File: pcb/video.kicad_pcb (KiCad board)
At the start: 4 copper layers, 159.9 x 99.9 mm, 174 parts, among them J1 09031966921, J3 Conn_01x06, J4 Conn_01x06, J5 Conn_01x06, J6 Conn_01x06, J7 DB15_Female_HighDensity, J8 HDMI_A, U1 NCP115, U10 NCA9306DPH, U2 LP3853ESX-3.3/NOPB, U3 LCMXO2-1200HC-4TG100I, U4 LCMXO2-7000HC-4TG144C, U5 THS8136, U6 TFP410PAP, U7 ESD224DQA, U8 ESD224DQA, U9 PCA9540BDP, X1 ASV-xxxMHz

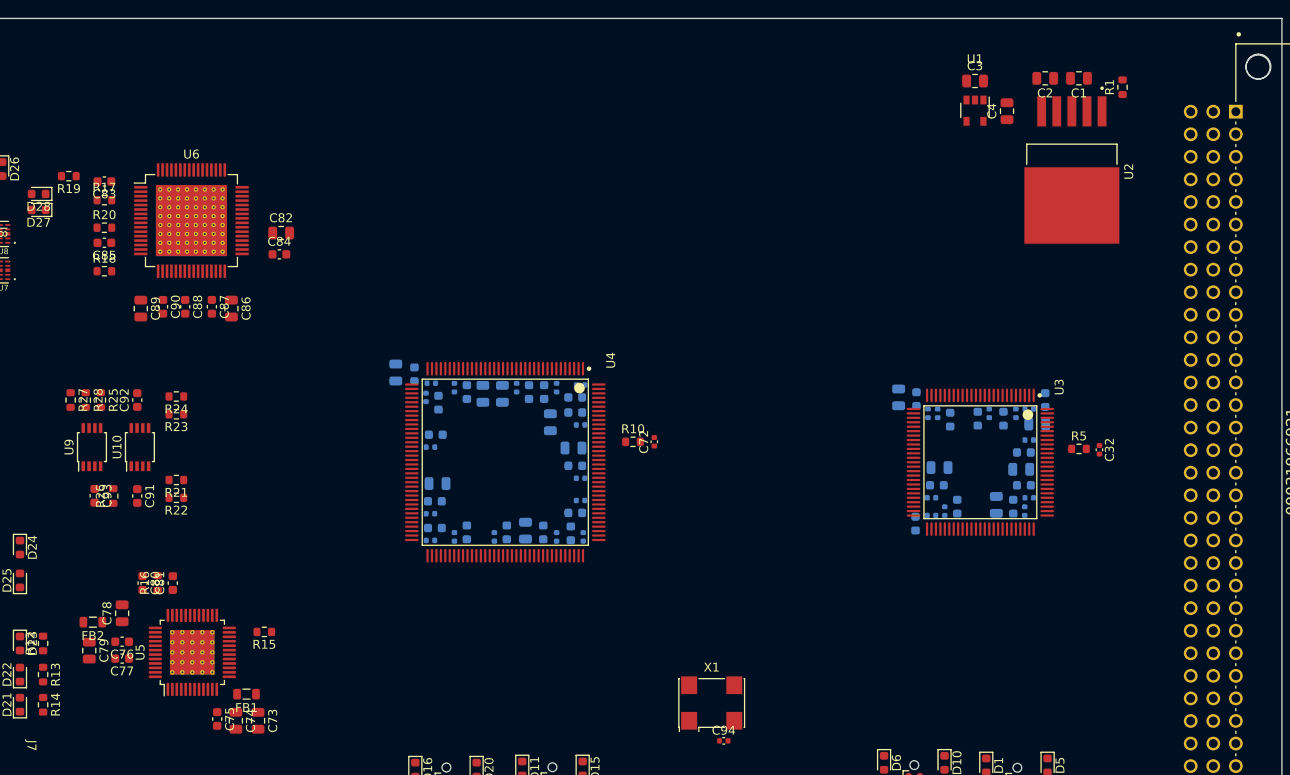
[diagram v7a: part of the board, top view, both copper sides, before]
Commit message: add traces from bus to bus controller
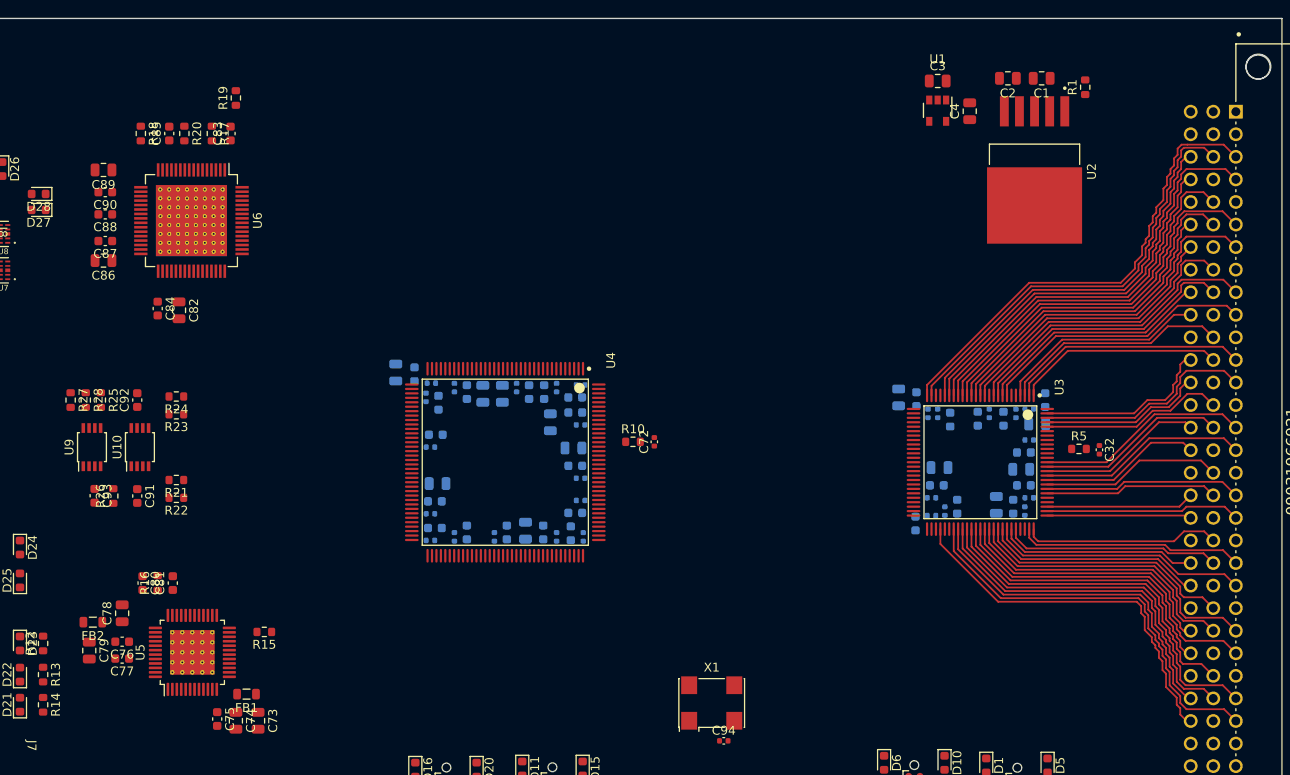
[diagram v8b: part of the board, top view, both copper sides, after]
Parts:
- moved R19 20.8 mm to (97.2, 54.0), turned to 90 degrees
- moved C89 16.2 mm to (82.3, 62.1), turned to 180 degrees
- moved R18 16.0 mm to (86.5, 58.0), turned to -90 degrees
- moved C86 15.4 mm to (82.3, 72.3), turned to 180 degrees
- moved C83 15.2 mm to (96.6, 58.0), turned to 90 degrees
- moved C84 15.0 mm to (88.4, 77.7), turned to -90 degrees
- moved C90 14.4 mm to (82.5, 64.6), turned to 180 degrees
- moved C82 14.4 mm to (90.8, 77.9), turned to -90 degrees
- moved C85 14.3 mm to (89.7, 58.0), turned to 90 degrees
- moved R17 14.2 mm to (94.5, 58.0), turned to -90 degrees
- moved C87 14.1 mm to (82.5, 70.1), turned to 180 degrees
- moved R20 13.9 mm to (91.4, 58.0), turned to -90 degrees
- moved C88 13.8 mm to (82.5, 67.1), turned to 180 degrees
- moved C1 4.20 mm to (187.9, 51.8)
- moved C2 4.20 mm to (184.1, 51.8)
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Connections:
- U3 pad 1: unconnected-(U3D-PL2C/L_GPLLT_IN) -> CONN_19
- U3 pad 10: unconnected-(U3D-PL4B) -> CONN_12
- U3 pad 12: unconnected-(U3D-PL5A/PCLKT3_1) -> CONN_11
- U3 pad 13: unconnected-(U3D-PL5B/PCLKC3_1) -> CONN_10
- U3 pad 14: unconnected-(U3D-PL5C) -> CONN_9
- U3 pad 15: unconnected-(U3D-PL5D) -> CONN_8
- U3 pad 16: unconnected-(U3D-PL8A) -> CONN_7
- U3 pad 17: unconnected-(U3D-PL8B) -> CONN_6
- U3 pad 18: unconnected-(U3D-PL8C) -> CONN_5
- U3 pad 19: unconnected-(U3D-PL8D) -> CONN_4
- U3 pad 2: unconnected-(U3D-PL2D/L_GPLLC_IN) -> CONN_18
- U3 pad 20: unconnected-(U3D-PL9A/PCLKT3_0) -> CONN_3
- U3 pad 21: unconnected-(U3D-PL9B/PCLKC3_0) -> CONN_2
- U3 pad 24: unconnected-(U3D-PL10C) -> CONN_1
- U3 pad 25: unconnected-(U3D-PL10D) -> CONN_0
- U3 pad 3: unconnected-(U3D-PL3A/PCLKT3_2) -> CONN_17
- U3 pad 4: unconnected-(U3D-PL3B/PCLKC3_2) -> CONN_16
- U3 pad 54: unconnected-(U3B-PR9C/(DQ1)) -> CONN_52
- U3 pad 57: unconnected-(U3B-PR9B/(DQ1)) -> CONN_51
- U3 pad 58: unconnected-(U3B-PR9A/(DQ1)) -> CONN_50
- U3 pad 59: unconnected-(U3B-PR8D/(DQ1)) -> CONN_49
- U3 pad 60: unconnected-(U3B-PR8C/(DQ1)) -> CONN_48
- U3 pad 61: unconnected-(U3B-PR8A/(DQS1)) -> CONN_47
- U3 pad 62: unconnected-(U3B-PR5D/PCLKC1_0/(DQ0)) -> CONN_46
- U3 pad 63: unconnected-(U3B-PR5C/PCLKT1_0/(DQ0)) -> CONN_45
- U3 pad 64: unconnected-(U3B-PR5B/(DQS0N)) -> CONN_44
- U3 pad 65: unconnected-(U3B-PR5A/(DQS0)) -> CONN_43
- U3 pad 66: unconnected-(U3B-PR4D/(DQ0)) -> CONN_42
- U3 pad 67: unconnected-(U3B-PR4C/(DQ0)) -> CONN_41
- U3 pad 68: unconnected-(U3B-PR4B/(DQ0)) -> CONN_40
- U3 pad 69: unconnected-(U3B-PR4A/(DQ0)) -> CONN_39
- U3 pad 7: unconnected-(U3D-PL3C) -> CONN_15
- U3 pad 70: unconnected-(U3B-PR3B/(DQ0)) -> CONN_38
- U3 pad 71: unconnected-(U3B-PR3A/(DQ0)) -> CONN_37
- U3 pad 74: unconnected-(U3B-PR2B/(DQ0)) -> CONN_36
- U3 pad 75: unconnected-(U3B-PR2A/(DQ0)) -> CONN_35
- U3 pad 76: unconnected-(U3A-PT17D/DONE) -> CONN_34
- U3 pad 77: unconnected-(U3A-PT17C/INITN) -> CONN_33
- U3 pad 78: unconnected-(U3A-PT16C) -> CONN_32
- U3 pad 8: unconnected-(U3D-PL3D) -> CONN_14
- U3 pad 81: unconnected-(U3A-PT15D/PROGRAMN) -> CONN_31
- U3 pad 82: unconnected-(U3A-PT15C/JTAGENB) -> CONN_30
- U3 pad 83: unconnected-(U3A-PT15B) -> CONN_29
- U3 pad 84: unconnected-(U3A-PT15A) -> CONN_28
- U3 pad 85: unconnected-(U3A-PT12D/SDA/PCLKC0_0) -> CONN_27
- U3 pad 86: unconnected-(U3A-PT12C/SCL/PCLKT0_0) -> CONN_26
- U3 pad 87: unconnected-(U3A-PT12B/PCLKC0_1) -> CONN_25
- U3 pad 88: unconnected-(U3A-PT12A/PCLKT0_1) -> CONN_24
- U3 pad 9: unconnected-(U3D-PL4A) -> CONN_13
- U3 pad 96: unconnected-(U3A-PT10B) -> CONN_23
- U3 pad 97: unconnected-(U3A-PT10A) -> CONN_22
- U3 pad 98: unconnected-(U3A-PT9B) -> CONN_21
- U3 pad 99: unconnected-(U3A-PT9A) -> CONN_20
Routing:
- net CONN_0: track 0.00 -> 52.8 mm
- net CONN_1: track 0.00 -> 49.4 mm
- net CONN_3: track 0.00 -> 48.6 mm
- net CONN_51: track 0.00 -> 46.3 mm
- net CONN_2: track 0.00 -> 44.6 mm
- net CONN_6: track 0.00 -> 43.5 mm
- net CONN_48: track 0.00 -> 43.1 mm
- net CONN_5: track 0.00 -> 43.0 mm
- net CONN_52: track 0.00 -> 42.7 mm
- net CONN_4: track 0.00 -> 41.7 mm
- net CONN_49: track 0.00 -> 41.1 mm
- net CONN_7: track 0.00 -> 40.1 mm
- net CONN_9: track 0.00 -> 39.8 mm
- net CONN_50: track 0.00 -> 39.1 mm
- net CONN_47: track 0.00 -> 38.0 mm
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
